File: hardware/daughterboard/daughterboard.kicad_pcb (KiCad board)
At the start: 4 copper layers, 51.1 x 51 mm, 90 parts, among them J1 Custom_PCIe_x4, U0 XTR200, U1 XTR200, U10 REF5030EIDR, U11 AD7193, U2 XTR200, U20 DAC80508Z, U3 XTR200, U4 XTR200, U5 XTR200, U6 XTR200, U7 XTR200, U8 SN74LV165, U9 AT21CS01

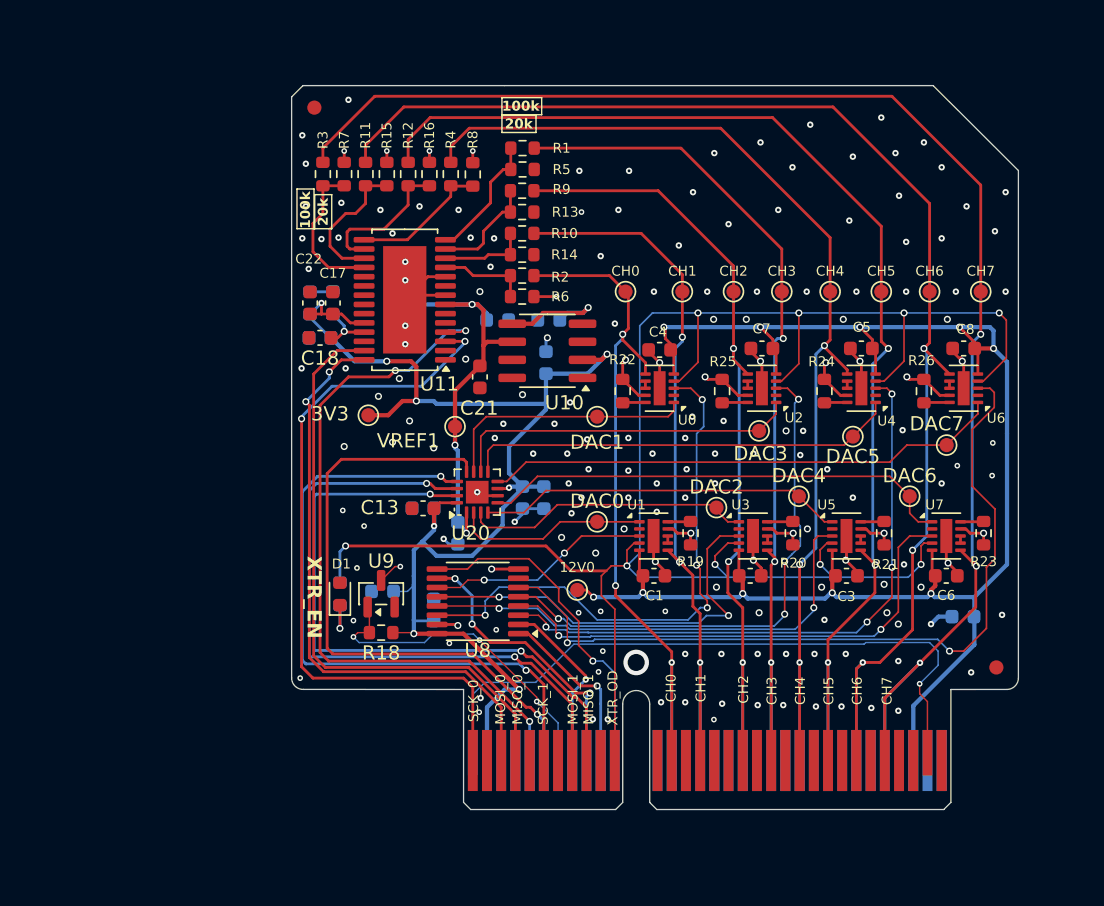
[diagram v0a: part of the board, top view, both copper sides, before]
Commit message: Rework AD7193 DVDD pi filter; resolve L1/R27 BOM TBDs
The DVDD filter (C17 - L1/R27 - C18) had all its local capacitance on the
unfiltered side: C22+C23+C17 = 1.2 uF on +3.3V, versus 100 nF on VDDA.

- Move C23 (1 uF) from +3.3V to VDDA. Zero BOM/placement change: it was
  already back-to-back with C18 at (87.50, 84.00). Filtered node goes
  100 nF -> 1.1 uF. Removed the stale +3.3V routing that ran through the
  pad, which would otherwise have shorted out L1 and R27.
- R27 1.5 -> 10 ohm. Corner 97 kHz -> 14 kHz for 4.2 mV drop; AD7193 DIDD
  is 0.4 mA (internal oscillator, no crystal fitted). Damping Q = 0.09.
- L1 resolved to C96708 (Sunlord GZ1608U601CTF, 600R@100MHz, 380 mohm,
  500 mA). The old "1.5 A" requirement was a phantom from the KiCad symbol
  name FerriteBead_0603_1.5A, not the design.
- R27 resolved to C144117 (YAGEO AF0603JR-0710RL, 10 ohm 5%).
- padne directives updated to match: r=10 on R27, r=0.38 on L1.
- Schematic note "Use NP0 for C17, C18" -> "Use X7R": 100 nF C0G does not
  exist in 0603 at 50 V, and these are supply shunts where C0G buys nothing.

master_bom_lcsc.csv (new file) additionally fixes:
- C9 was grouped on the 10 uF line but is 0.1 uF; moved to the 100 nF line.
  100 nF 152 -> 160 units, 10 uF 16 -> 8 units.
- R18 row had an unquoted comma splitting it into 18 CSV fields.
- Totals: 717.34 -> 717.70, LCSC 308.88 -> 307.38.

Co-Authored-By: Claude Opus 5 <noreply@anthropic.com>
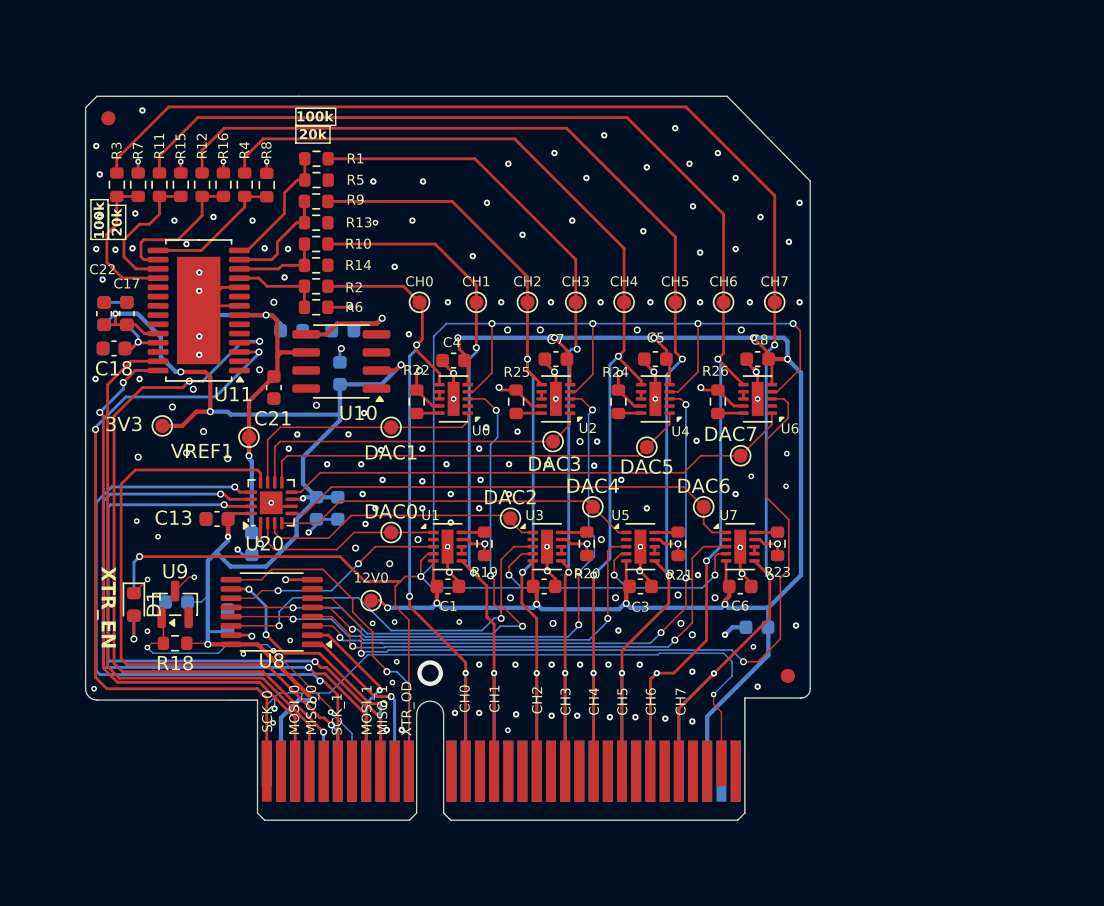
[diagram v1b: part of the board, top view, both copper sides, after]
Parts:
- C9: value 10uF -> 0.1uF
- R17: value 100k -> 500
- R19, R20, R21, R22, R23, R24, R25, R26: value 5k -> 4.7k
- R27: value 1.5 -> 10
- U10: value REF5030EIDR -> REF5030IDGKR
- U20: value DAC80508Z -> DAC80508ZR
- moved FID2 14.7 mm to (134.9, 107.0)
- moved C5 14.5 mm to (125.6, 84.8)
- moved C7 14.5 mm to (118.6, 84.8)
- moved CH2 14.5 mm to (116.6, 80.8)
- moved U2 14.5 mm to (118.6, 87.5)
- moved U3 14.5 mm to (118.0, 98.0)
- moved U4 14.5 mm to (125.6, 87.5)
- moved 12V0 14.5 mm to (105.6, 101.8)
- moved 3V3 14.5 mm to (90.9, 89.5)
- moved C1 14.5 mm to (111.0, 100.8)
- moved C10 14.5 mm to (103.6, 82.8)
- moved C11 14.5 mm to (103.4, 85.8)
- moved C12 14.5 mm to (103.2, 95.2)
- moved C13 14.5 mm to (94.7, 96.0)
- moved C14 14.5 mm to (93.4, 81.7)
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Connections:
- C23 pad 1: +3.3V -> VDDA
- D1 pad 1: Net-(D1-K) -> GND
- D1 pad 2: GND -> Net-(D1-A)
- R17 pad 1: Net-(D1-K) -> Net-(D1-A)
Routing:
- net Net-(D1-K): track 3.24 -> 0.00 mm, vias 1 -> 0
- net Net-(D1-A): track 0.00 -> 3.24 mm, vias 0 -> 1
- net GND: track 76.4 -> 77.7 mm, vias 182 -> 191
- net VDDA: track 4.06 -> 5.17 mm
- net +3.3V: track 92.7 -> 93.3 mm
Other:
- board size 51.1 x 51 mm -> 51 x 51 mm

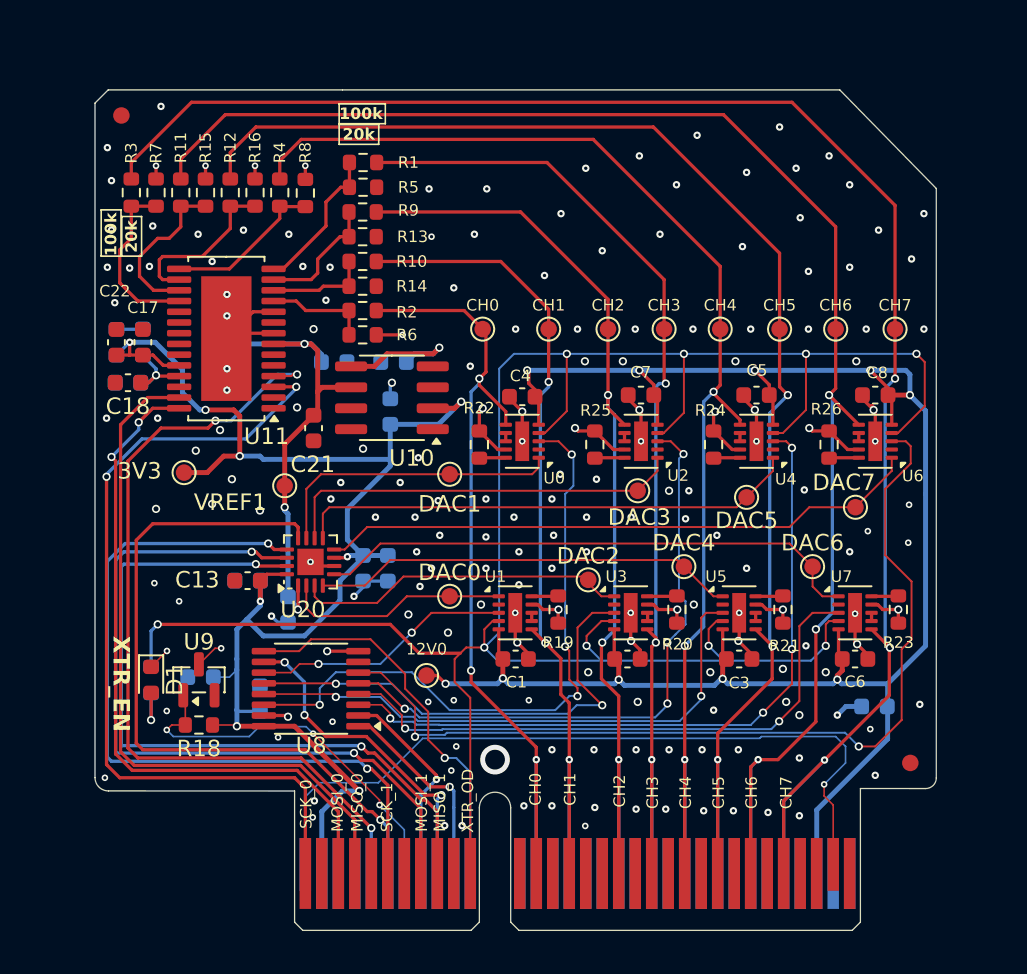
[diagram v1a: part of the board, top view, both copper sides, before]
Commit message: OPA2333 sense buffers and XTR200 EF fault-detection chain
Two daughterboard revisions plus the firmware to drive them.

OPA2333 sense buffers (root-causes the 3 mV offset):
- The ~3 mV offset seen during the 8-board test was the AD7193's *internal*
  input buffer. With the 6:1 divider, a low-current channel's ADC input sits
  below the buffered mode's usable common-mode range, so the buffer added a
  systematic offset instead of tracking.
- Fixed by disabling it (CONF.BUF = 0) and adding 8 external unity-gain
  followers: U13-U16 (OPA2333, 2 ch per package) between the divider taps and
  the ADC inputs, with R28-R35 1k series and C26-C33 100nF anti-alias
  (corner 1.59 kHz; was 339 kHz at 100R/4.7nF, which attenuated neither the
  OPA333 chop nor the AD7193 modulator rate).

XTR200 EF fault detection:
- Each daughterboard's SN74LV165 (U8) samples its eight XTR200 EF pins; the
  motherboard daisy-chains all eight into one 64-bit register on a private
  bit-banged 3-wire bus (CP=GP16, Q7=GP17, PL=GP18), so reading it never
  disturbs SPI0 (ADC + '595) or SPI1 (DAC).
- New EFChain.cpp/.h; loop() polls every 20 ms, latches a new fault, zeroes
  that channel's DAC and pins it at 0 mA until FAULTCLR.
- New host commands: FAULT?, FAULTCLR, FAULTEN ON|OFF.
- Documented limits: EF is one shared flag (open / saturation / SET short /
  UVLO <8 V / >150 C); open detection only arms above IOUT ~0.75 mA with
  RSET = 4.7k; an unpopulated slot breaks the chain, so efValidMask() reports
  which boards' bits are trustworthy.

Also:
- master_bom_lcsc.csv: U13-U16 and R28-R35 rows added (both LCSC-TBD), 100nF
  line 160 -> 224 units for C26-C33. Total understated until the OPA2333 line
  is priced.
- README: 3 mV offset moved from open issue to resolved.
- motherboard.kicad_pcb: 64 further routed segments.
- padne_plots_layers.py: per-layer padne plotting helper.
- paper/todo.txt: working notes.

Co-Authored-By: Claude Opus 5 <noreply@anthropic.com>
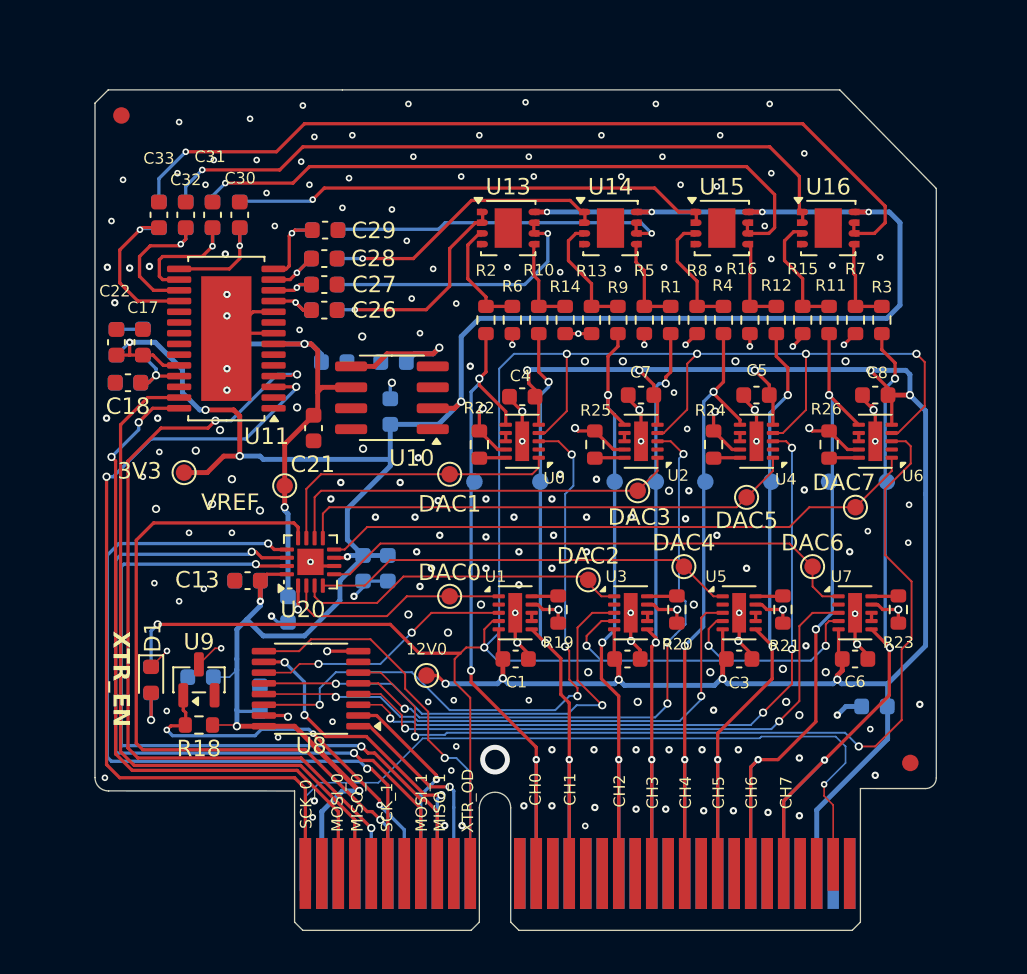
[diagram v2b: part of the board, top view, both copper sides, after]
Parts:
- added C26: 100nF, Capacitor_SMD:C_0603_1608Metric, F.Cu at (99.4, 79.6)
- added C27: 100nF, Capacitor_SMD:C_0603_1608Metric, F.Cu at (99.4, 78.0)
- added C28: 100nF, Capacitor_SMD:C_0603_1608Metric, F.Cu at (99.4, 76.5)
- added C29: 100nF, Capacitor_SMD:C_0603_1608Metric, F.Cu at (99.5, 74.8)
- added C30: 100nF, Capacitor_SMD:C_0603_1608Metric, F.Cu at (94.3, 73.8)
- added C31: 100nF, Capacitor_SMD:C_0603_1608Metric, F.Cu at (92.6, 73.8)
- added C32: 100nF, Capacitor_SMD:C_0603_1608Metric, F.Cu at (91.0, 73.8)
- added C33: 100nF, Capacitor_SMD:C_0603_1608Metric, F.Cu at (89.4, 73.8)
- added R28: 1k, Resistor_SMD:R_0603_1608Metric, B.Cu at (99.4, 79.6)
- added R29: 1k, Resistor_SMD:R_0603_1608Metric, B.Cu at (99.4, 78.0)
- added R30: 1k, Resistor_SMD:R_0603_1608Metric, B.Cu at (99.4, 76.5)
- added R31: 1k, Resistor_SMD:R_0603_1608Metric, B.Cu at (99.5, 74.8)
- added R32: 1k, Resistor_SMD:R_0603_1608Metric, B.Cu at (94.3, 73.8)
- added R33: 1k, Resistor_SMD:R_0603_1608Metric, B.Cu at (92.6, 73.8)
- added R34: 1k, Resistor_SMD:R_0603_1608Metric, B.Cu at (91.0, 73.8)
- added R35: 1k, Resistor_SMD:R_0603_1608Metric, B.Cu at (89.4, 73.8)
- added U13: OPA2333xxDRB, Package_SON:Texas_S-PVSON-N8, F.Cu at (110.5, 74.6)
- added U14: OPA2333xxDRB, Package_SON:Texas_S-PVSON-N8, F.Cu at (116.8, 74.6)
- added U15: OPA2333xxDRB, Package_SON:Texas_S-PVSON-N8, F.Cu at (123.5, 74.6)
- added U16: OPA2333xxDRB, Package_SON:Texas_S-PVSON-N8, F.Cu at (129.9, 74.6)
- CH0, CH1, CH2, CH3, CH4, CH5, CH6, CH7: moved to B.Cu
- moved R3 46.2 mm to (133.2, 80.2), turned to -90 degrees
- moved R7 43.1 mm to (131.6, 80.2), turned to 90 degrees
- moved R11 40.1 mm to (130.0, 80.2), turned to -90 degrees
- moved R15 37.0 mm to (128.4, 80.2), turned to 90 degrees
- moved R12 34.0 mm to (126.8, 80.2), turned to -90 degrees
- moved R16 31.0 mm to (125.2, 80.2), turned to 90 degrees
- moved R4 28.0 mm to (123.6, 80.2), turned to -90 degrees
- moved R8 25.0 mm to (122.0, 80.2), turned to 90 degrees
- moved R1 21.0 mm to (120.4, 80.2), turned to -90 degrees
- moved R5 18.9 mm to (118.8, 80.2), turned to 90 degrees
- moved R9 16.8 mm to (117.2, 80.2), turned to -90 degrees
- moved R13 14.8 mm to (115.6, 80.2), turned to 90 degrees
- moved R14 12.4 mm to (114.0, 80.2), turned to 90 degrees
- moved R10 11.2 mm to (112.4, 80.2), turned to -90 degrees
- moved CH4 9.29 mm to (122.5, 90.0), turned to 180 degrees
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- renumbered VREF1 to VREF
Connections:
- R1 pad 1: CH3_V -> CH3_B
- R10 pad 1: CH1_V -> CH1_B
- R11 pad 1: CH6_V -> CH6_B
- R12 pad 1: CH5_V -> CH5_B
- R13 pad 2: CH2_V -> CH2_B
- R14 pad 2: CH1_V -> CH1_B
- R15 pad 2: CH6_V -> CH6_B
- R16 pad 2: CH5_V -> CH5_B
- R2 pad 1: CH0_V -> CH0_B
- R3 pad 1: CH7_V -> CH7_B
- R4 pad 1: CH4_V -> CH4_B
- R5 pad 2: CH3_V -> CH3_B
- R6 pad 2: CH0_V -> CH0_B
- R7 pad 2: CH7_V -> CH7_B
- R8 pad 2: CH4_V -> CH4_B
- R9 pad 1: CH2_V -> CH2_B
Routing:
- net +3.3V: track 93.3 -> 154.4 mm, vias 8 -> 12
- net CH7: track 104.4 -> 45.6 mm
- net Net-(U16B--): track 0.00 -> 52.7 mm, vias 0 -> 1
- net CH6: track 96.7 -> 45.4 mm
- net CH5: track 86.8 -> 43.3 mm
- net Net-(U16A--): track 0.00 -> 42.6 mm, vias 0 -> 1
- net Net-(U15B--): track 0.00 -> 40.1 mm, vias 0 -> 1
- net CH4: track 78.8 -> 43.3 mm
- net Net-(U15A--): track 0.00 -> 29.3 mm, vias 0 -> 1
- net CH3: track 64.8 -> 41.5 mm
- net Net-(U14B--): track 0.00 -> 21.0 mm, vias 0 -> 1
- net CH2: track 61.1 -> 43.0 mm
- net Net-(U14A--): track 0.00 -> 17.2 mm, vias 0 -> 1
- net Net-(U13B--): track 0.00 -> 16.4 mm, vias 0 -> 1
- net Net-(U13A--): track 0.00 -> 13.0 mm, vias 0 -> 1
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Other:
- board text removed: "100k"
- board text removed: "20k"

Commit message: daughterboard: add silkscreen logos, refill zones
Two LOGO footprints and the resulting zone refill. No netlist or
component changes.

Co-Authored-By: Claude Opus 5 <noreply@anthropic.com>
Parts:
- added G***: LOGO, LOGO, B.Cu at (128.3, 76.2)
- added G***: LOGO, LOGO, B.Cu at (121.4, 72.8)
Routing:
- net +12V: track 114.9 -> 115.4 mm
- net GND: vias 206 -> 217
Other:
- board text removed: "JLCJLCJLCJLC"
